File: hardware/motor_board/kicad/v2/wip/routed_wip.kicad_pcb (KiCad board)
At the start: 4 copper layers, 85 x 35 mm, 232 parts, among them J1 BOOMELE_1.27-2x10P, J2 BM06B-SRSS-TB, J3 BM06B-SRSS-TB, J4 B5B-XH-A, Q1 HYG015N04LS1C2, Q2 HYG015N04LS1C2, Q3 HYG015N04LS1C2, Q4 HYG015N04LS1C2, Q5 HYG015N04LS1C2, Q6 HYG015N04LS1C2, Q7 HYG015N04LS1C2, Q8 HYG015N04LS1C2, U1 STM32G474RET6, U10 SN74LVC3G17DCUR, U11 TPS22945DCKR, U12 TPS22945DCKR, U13 LM74502DDFR, U14 74LVC1G17SE-7, U2 DRV8323RHRGZR, U3 DRV8316CRRGFR, U4 DRV8316CRRGFR, U5 AP2112K-3.3TRG1, U6 SN74LVC08ABQAR, U7 INA239AIDGSR, U8 BQ76907RGRR, U9 SN74LVC3G17DCUR

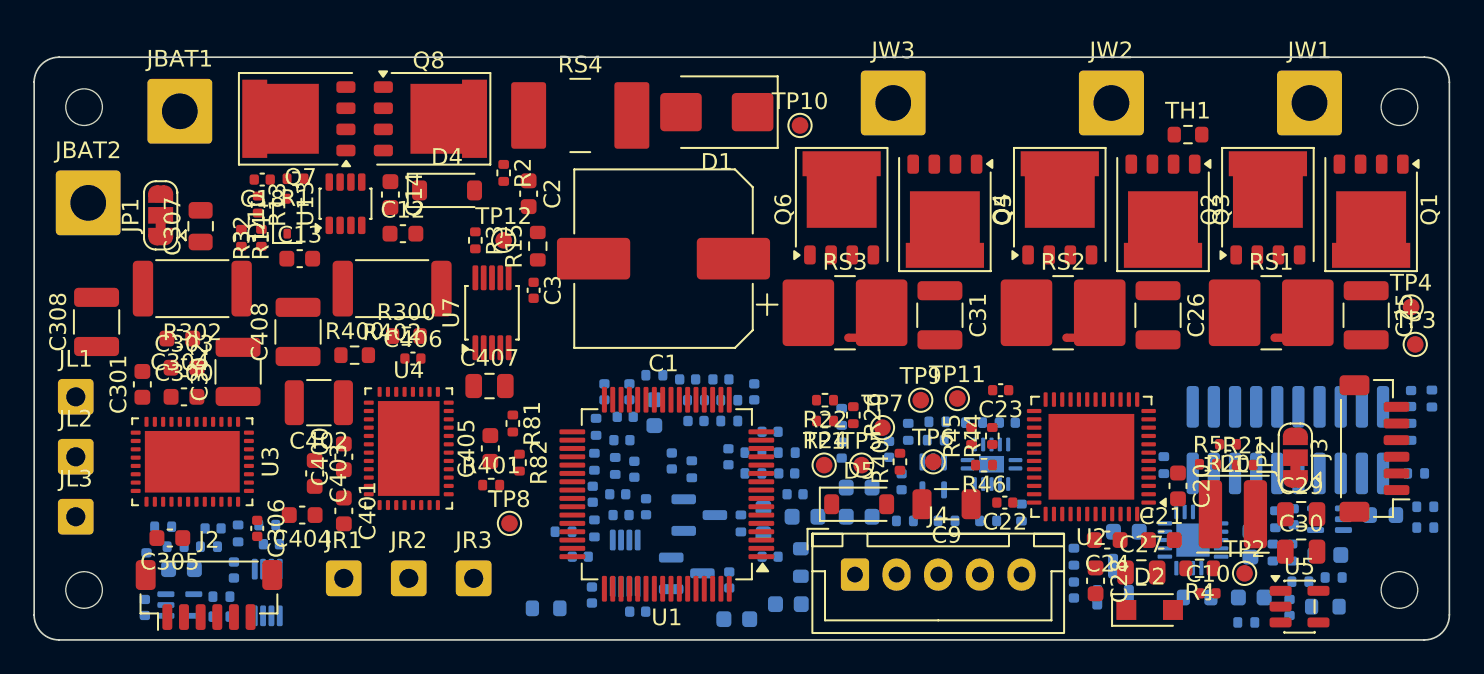
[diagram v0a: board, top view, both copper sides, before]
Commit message: v2 scripted pre-routing of the remaining clusters: v2_ilock (weapon interlock / U2 control, 27 nets), v2_sense (sensor front ends + dividers, 24 nets), v2_rear (J1 side, BMS, INA, 20 nets); DRC 0; 22 signal/rail nets still open (+3V3/+5V branches, CELL0-4, SWD, UART, U7 ALERT, 4 left-sensor lines, W_NTC); WIP routed board in kicad/v2/wip/; router: analog L3/L4 rule options; fr_watch.py
Co-Authored-By: Claude Opus 5.5 (1M context) <noreply@anthropic.com>
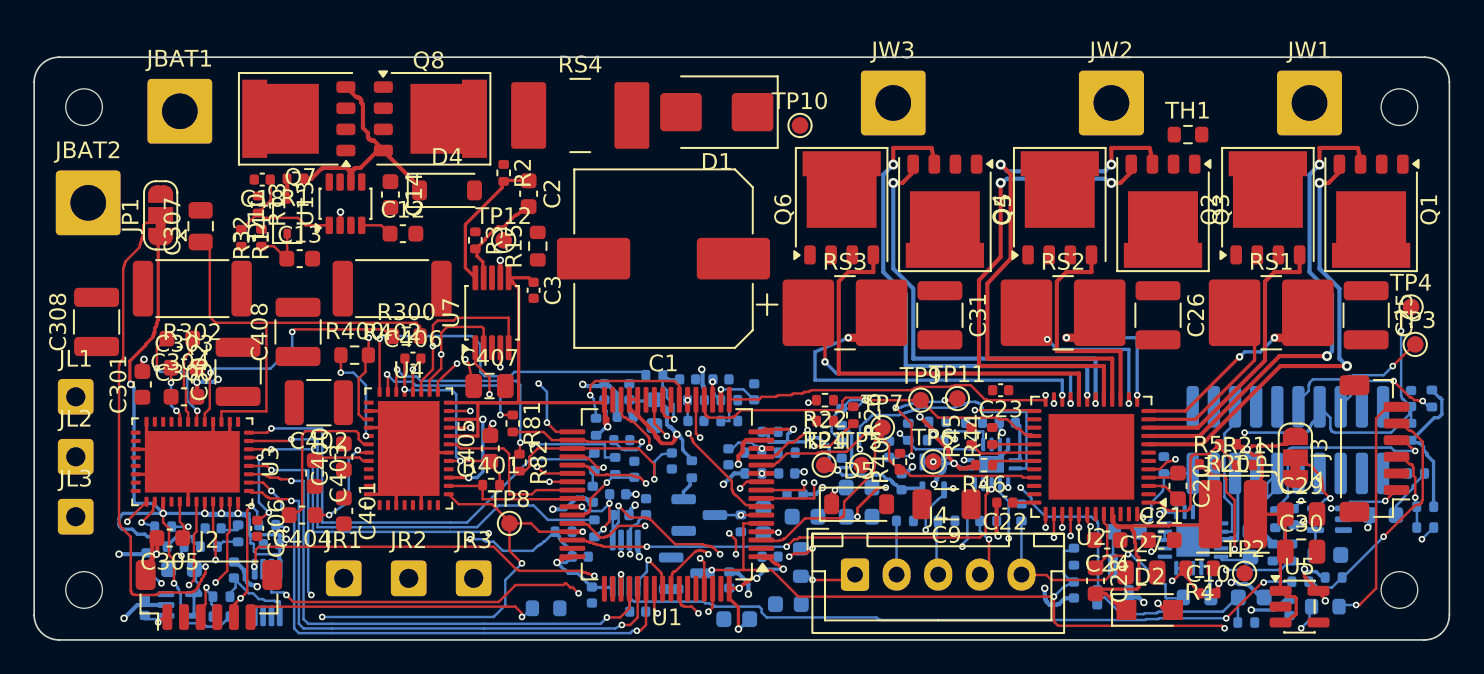
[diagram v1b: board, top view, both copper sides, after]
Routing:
- net +3V3: track 0.00 -> 188.7 mm, vias 0 -> 21
- net GND: track 0.00 -> 71.2 mm, vias 0 -> 36
- net /mcu/NRST: track 0.00 -> 66.0 mm, vias 0 -> 3
- net SPI_MOSI: track 0.00 -> 60.1 mm, vias 0 -> 3
- net SPI_SCK: track 0.00 -> 59.8 mm, vias 0 -> 3
- net /sensors/R_H1B: track 0.00 -> 57.3 mm, vias 0 -> 3
- net SPI_MISO: track 0.00 -> 56.9 mm, vias 0 -> 4
- net +5V: track 0.00 -> 54.6 mm, vias 0 -> 4
- net /sensors/R_H2B: track 0.00 -> 46.4 mm, vias 0 -> 2
- net R_MTEMP: track 0.00 -> 45.9 mm, vias 0 -> 4
- net DRV_OFF: track 0.00 -> 44.8 mm, vias 0 -> 4
- net /sensors/R_H3B: track 0.00 -> 43.0 mm, vias 0 -> 2
- net L_nFAULT: track 0.00 -> 39.5 mm, vias 0 -> 2
- net L_nCS: track 0.00 -> 37.2 mm, vias 0 -> 3
- net L_INHC: track 0.00 -> 37.2 mm, vias 0 -> 2
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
